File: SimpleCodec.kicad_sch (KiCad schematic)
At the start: 1 part

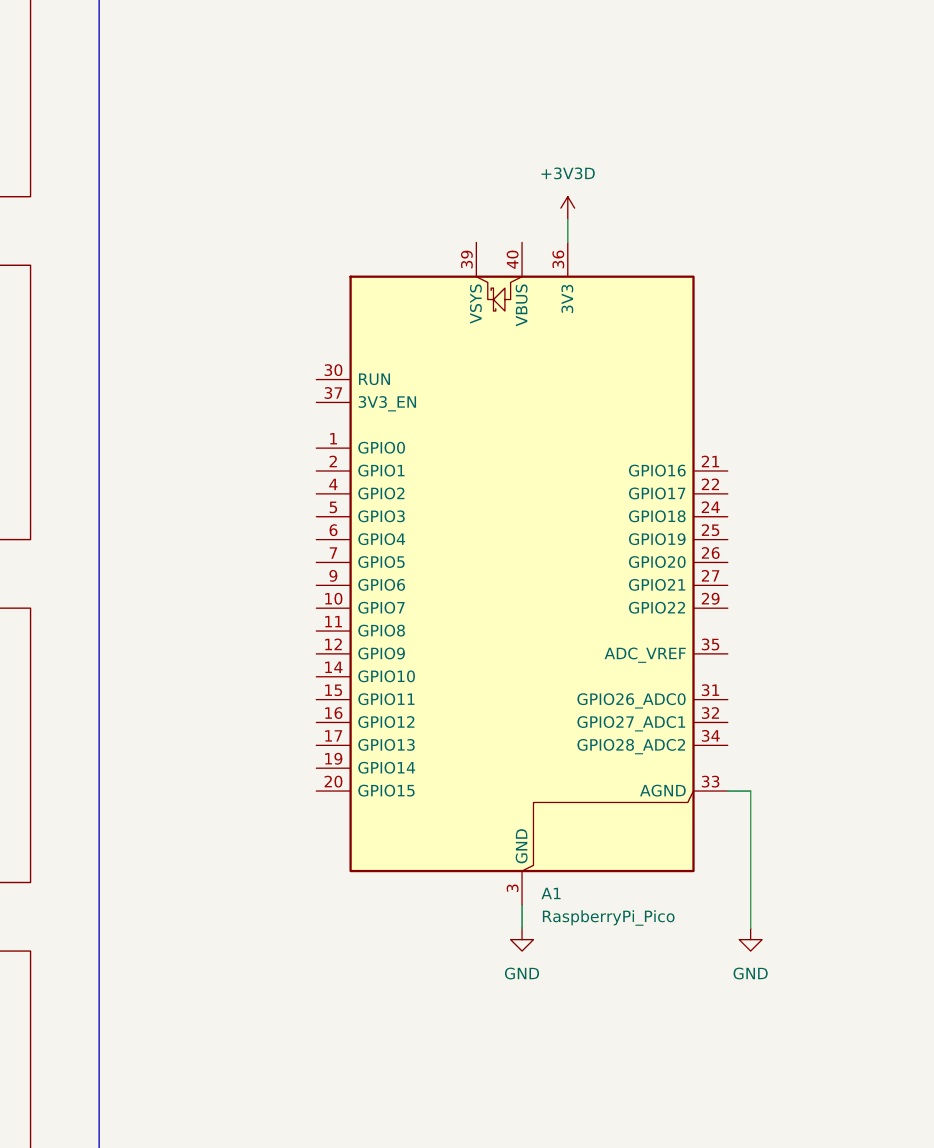
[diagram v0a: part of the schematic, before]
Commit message: Schematic
Updated the schematic.
Added the codec schematic module.
Added the buffer schematic module.
Added the RP2350 schematic module.
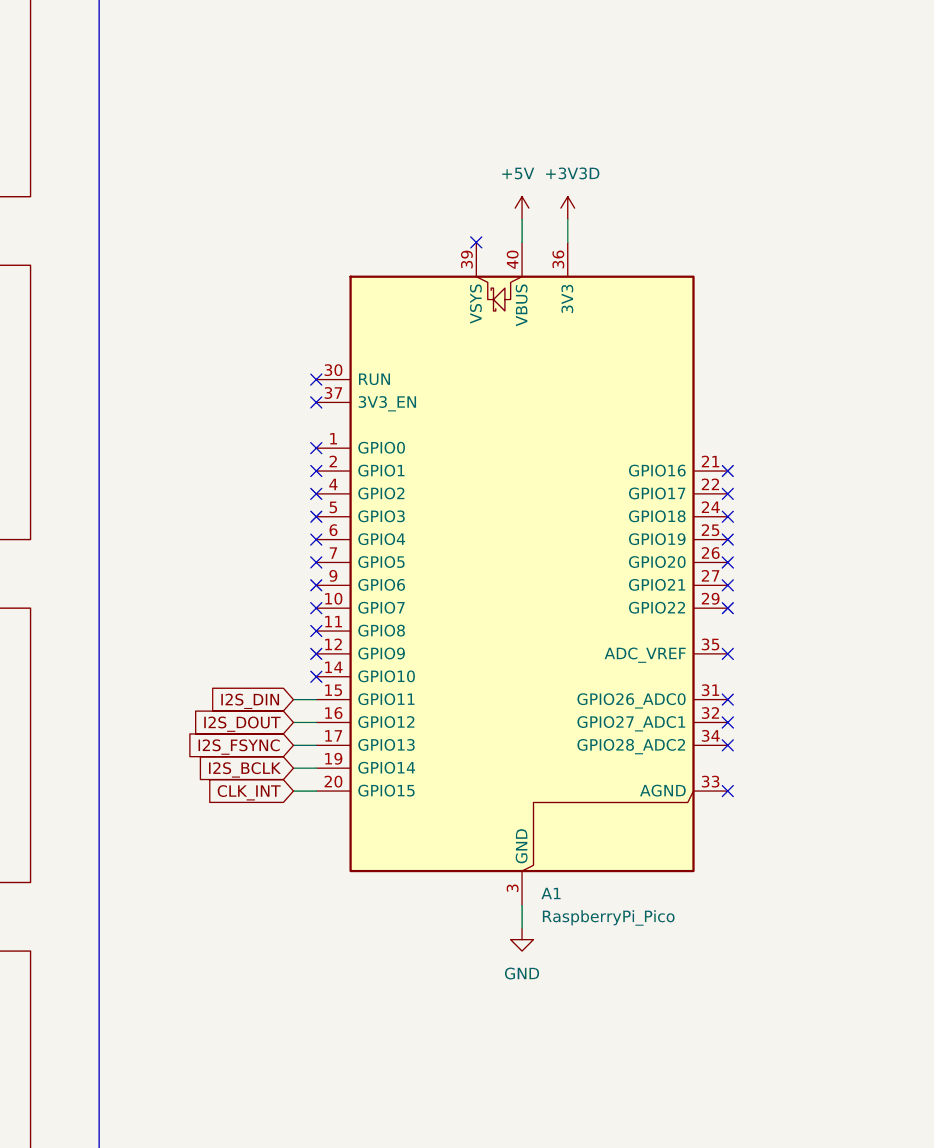
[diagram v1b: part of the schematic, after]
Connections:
- net GND: no longer A1.33 (AGND)
- net I2S_DIN: now reaches A1.15 (GPIO11)
- net I2S_DOUT: now reaches A1.16 (GPIO12)
- net I2S_FSYNC: now reaches A1.17 (GPIO13)
- net I2S_BCLK: now reaches A1.19 (GPIO14)
- net CLK_INT: now reaches A1.20 (GPIO15)
- net +5V: now reaches A1.40 (VBUS)
- no-connect marks 0 -> 26

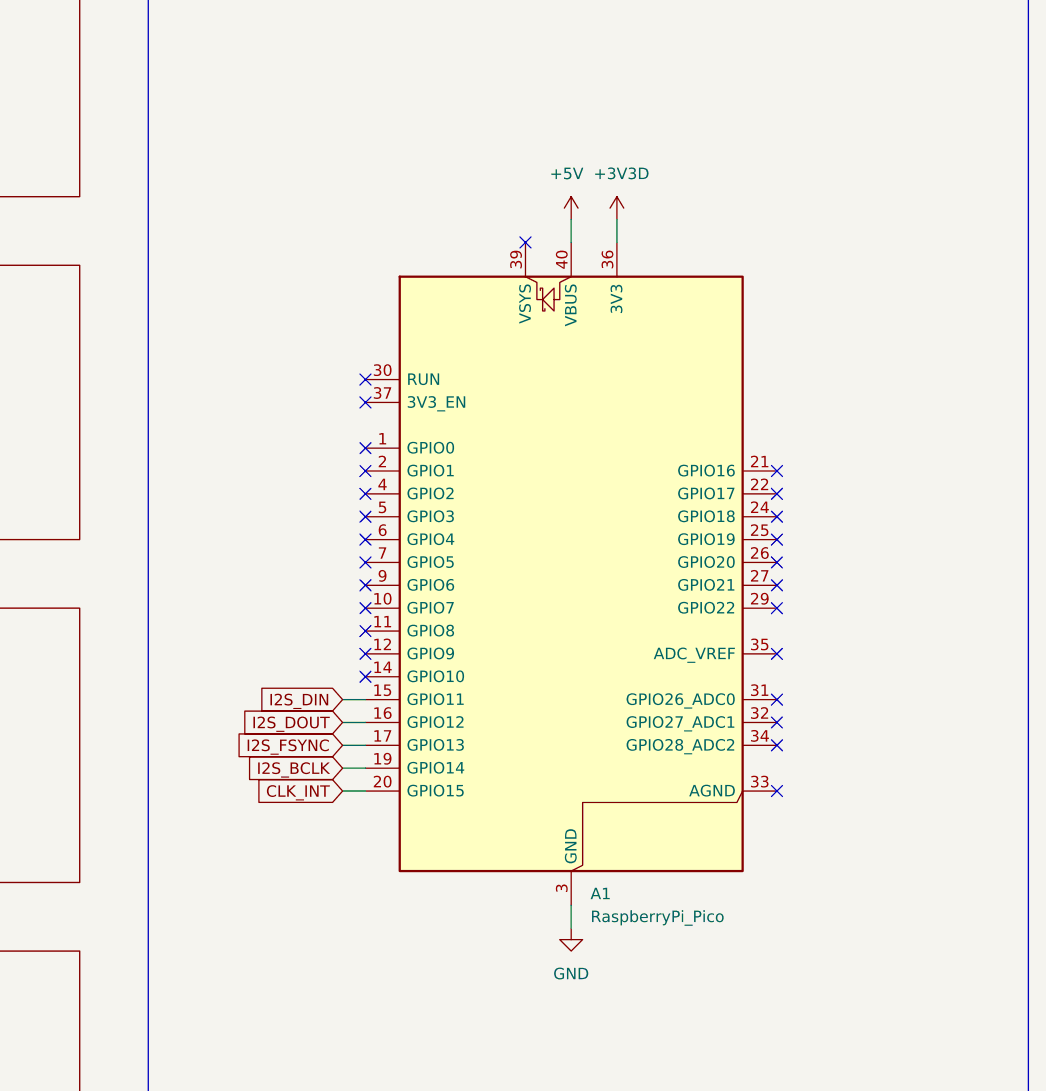
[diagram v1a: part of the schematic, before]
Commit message: Schematic
Updated the power delivery module.
Other minor changes.
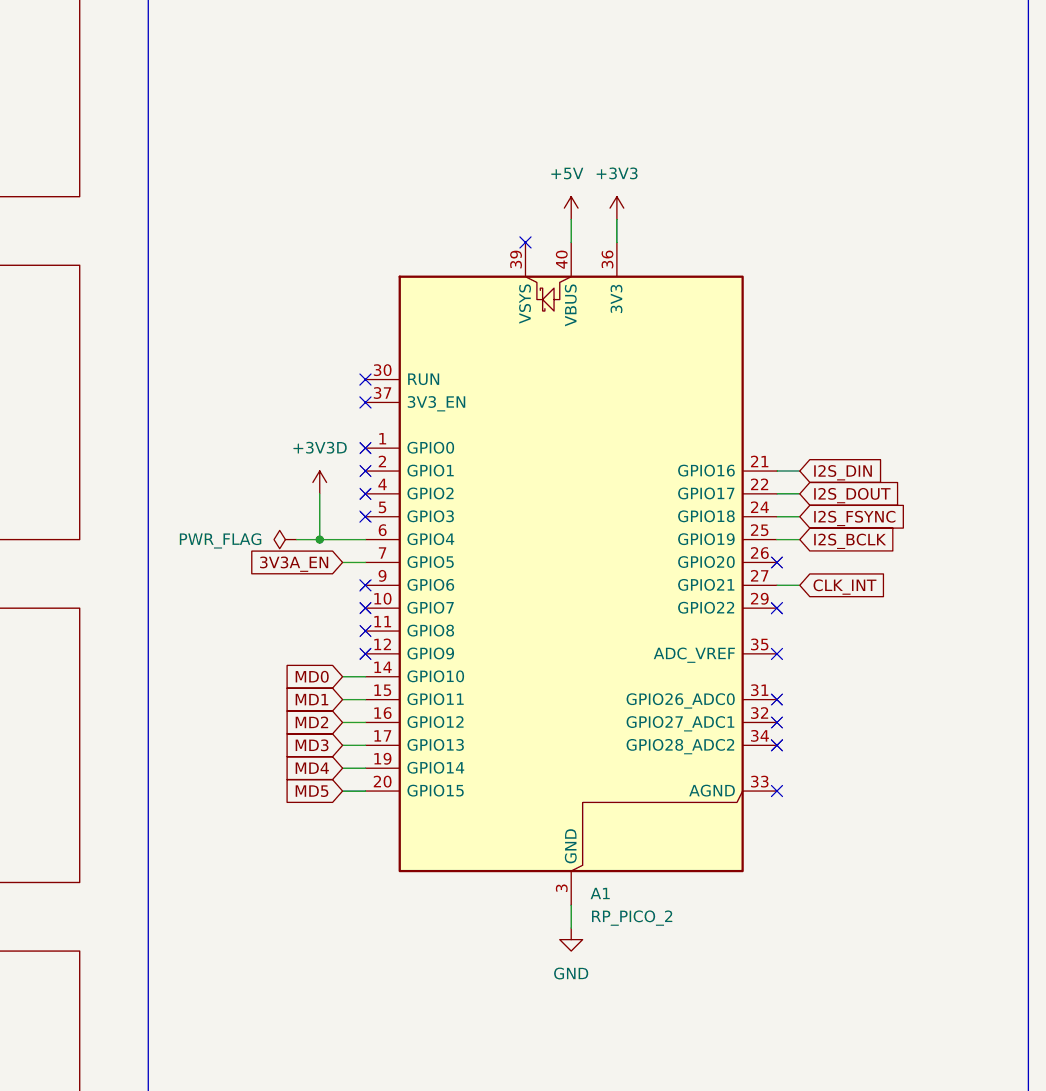
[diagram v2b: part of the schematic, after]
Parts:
- removed A1: RaspberryPi_Pico, Module:RaspberryPi_Pico_Common_THT, symbol MCU_Module:RaspberryPi_Pico
- added A1: RP_PICO_2, Custom_Parts:RP_PICO_2_THT, symbol Custom_Parts:RP_PICO_2
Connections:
- net +3V3D: now also A1.6 (GPIO4)
- net +5V: now also A1.40 (VBUS)
- net CLK_INT: now also A1.27 (GPIO21)
- net GND: now also A1.13 (GND), A1.18 (GND), A1.23 (GND), A1.28 (GND), A1.3 (GND), A1.38 (GND), A1.8 (GND)
- net I2S_BCLK: now also A1.25 (GPIO19)
- net I2S_DIN: now also A1.21 (GPIO16)
- net I2S_DOUT: now also A1.22 (GPIO17)
- net I2S_FSYNC: now also A1.24 (GPIO18)
- new net +3V3: A1.36 (3V3)
- new net 3V3A_EN: A1.7 (GPIO5)
- new net MD0: A1.14 (GPIO10)
- new net MD1: A1.15 (GPIO11)
- new net MD2: A1.16 (GPIO12)
- new net MD3: A1.17 (GPIO13)
- new net MD4: A1.19 (GPIO14)
- new net MD5: A1.20 (GPIO15)
- no-connect marks 26 -> 18

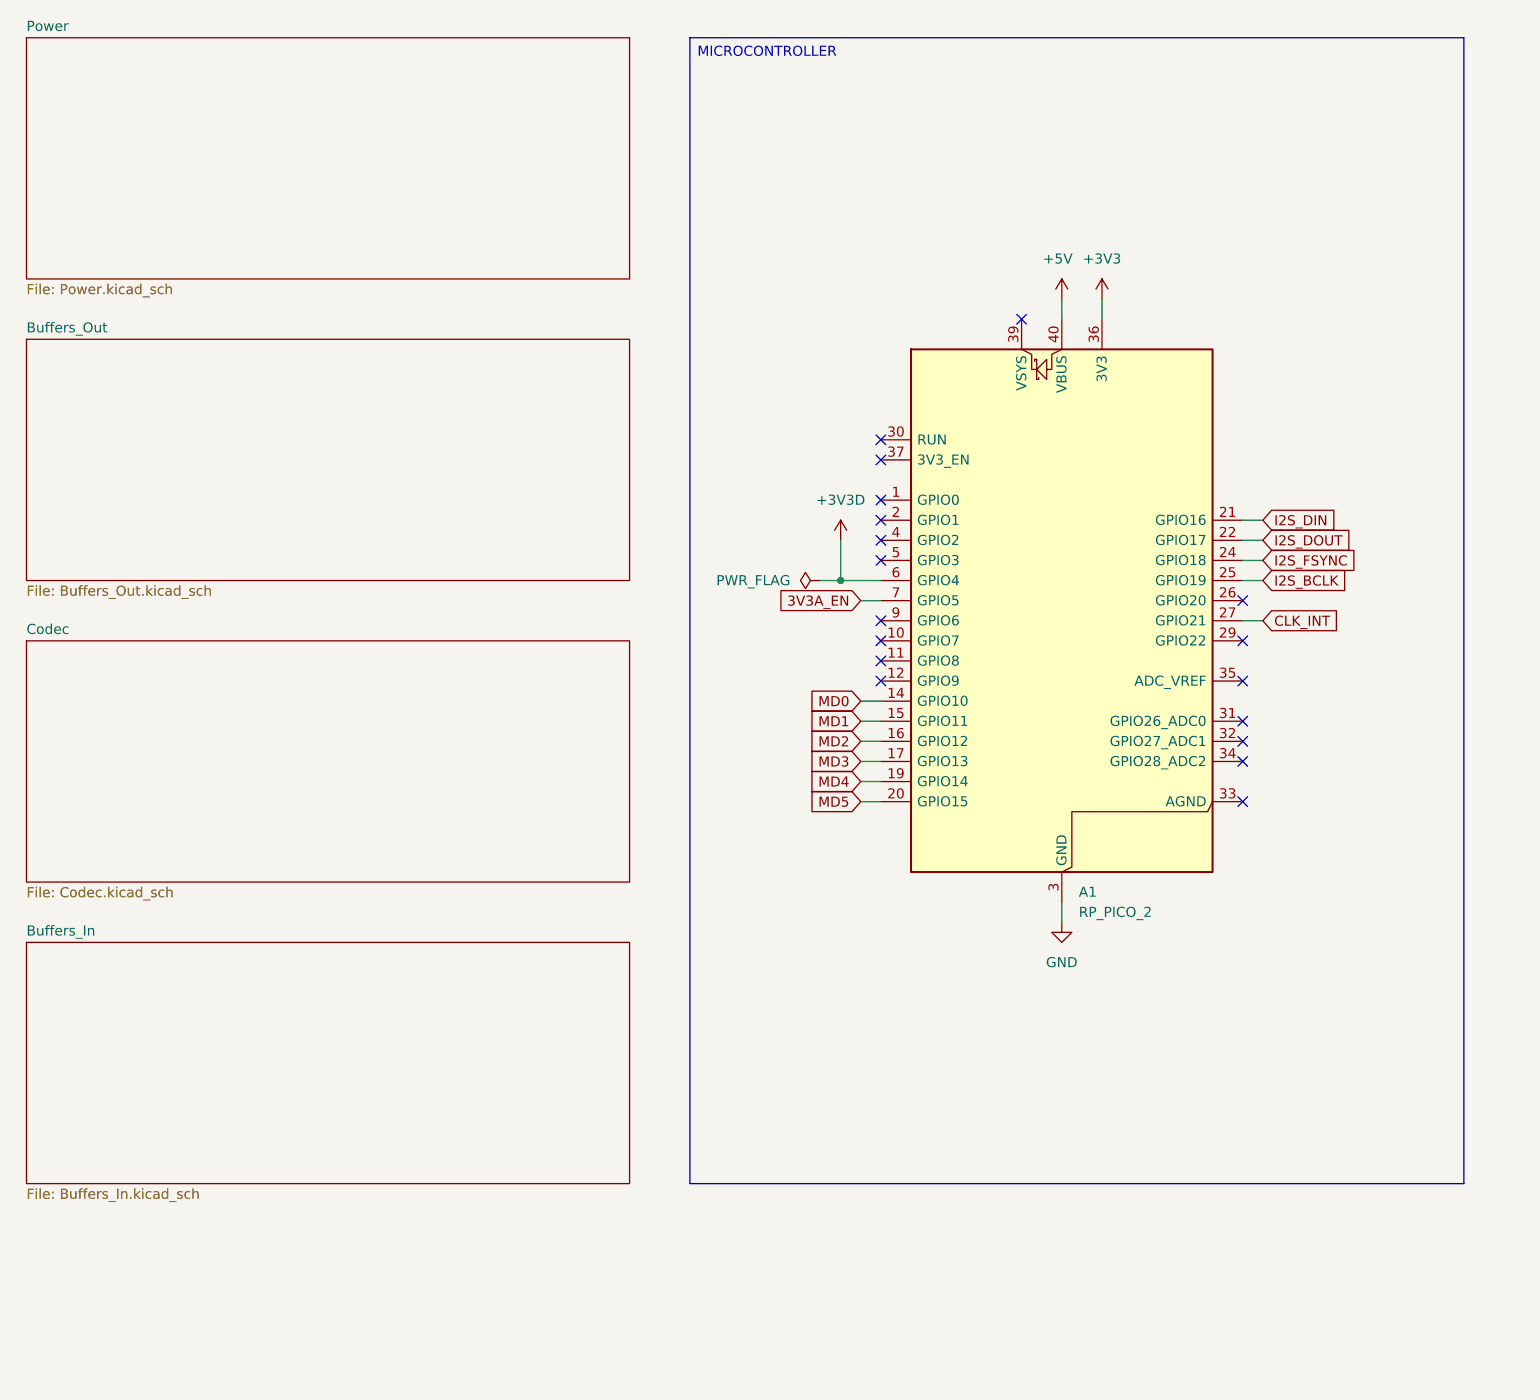
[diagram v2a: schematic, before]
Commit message: Moved to a CS4272 codec as a cheaper alternative with similar performance.
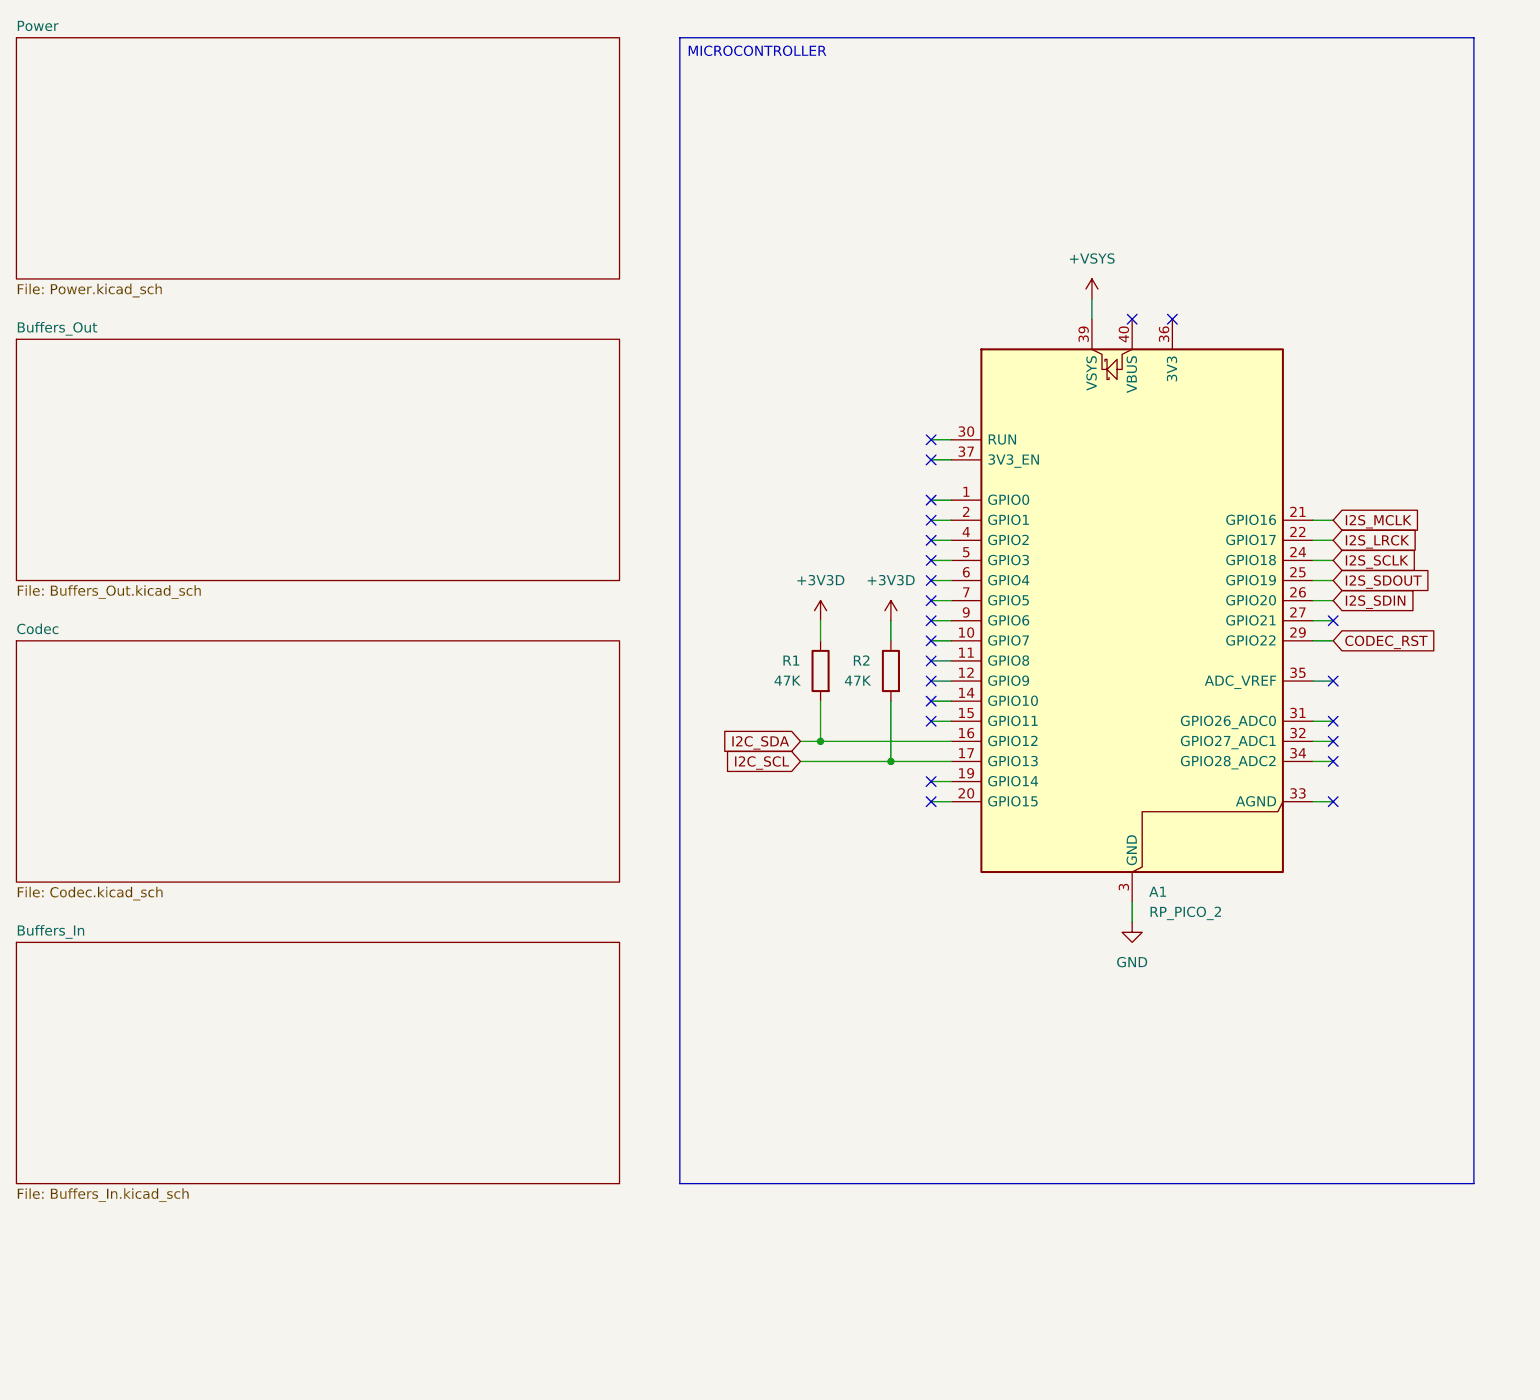
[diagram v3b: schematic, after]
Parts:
- added R1, R2: 47K, Resistor_SMD:R_0603_1608Metric, symbol Device:R
- A1: footprint Custom_Parts:RP_PICO_2_THT -> Custom_Parts:RP_PICO_2_SMD
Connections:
- net +3V3D: now also R1.1, R2.1; no longer A1.6 (GPIO4)
- net I2S_SDIN: now reaches A1.26 (GPIO20)
- net CODEC_RST: now reaches A1.29 (GPIO22)
- net +VSYS: now reaches A1.39 (VSYS)
- net +3V3: no longer names the net of A1.36 (3V3)
- net +5V: no longer names the net of A1.40 (VBUS)
- net 3V3A_EN: no longer names the net of A1.7 (GPIO5)
- net CLK_INT: no longer names the net of A1.27 (GPIO21)
- net I2S_BCLK renamed I2S_SDOUT
- net I2S_DIN renamed I2S_MCLK
- net I2S_DOUT renamed I2S_LRCK
- net I2S_FSYNC renamed I2S_SCLK
- net MD0: no longer names the net of A1.14 (GPIO10)
- net MD1: no longer names the net of A1.15 (GPIO11)
- net MD2 renamed I2C_SDA
- net I2C_SDA: now also R1.2
- net MD3 renamed I2C_SCL
- net I2C_SCL: now also R2.2
- net MD4: no longer names the net of A1.19 (GPIO14)
- net MD5: no longer names the net of A1.20 (GPIO15)
- no-connect marks 18 -> 24
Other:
- moved on the sheet: A1
